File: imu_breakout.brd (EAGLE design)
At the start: 29.5 x 20.7 mm, 11 parts, among them IC1 FT232RL, U1 AHRS8P_CONN, U2 USB-MICROB

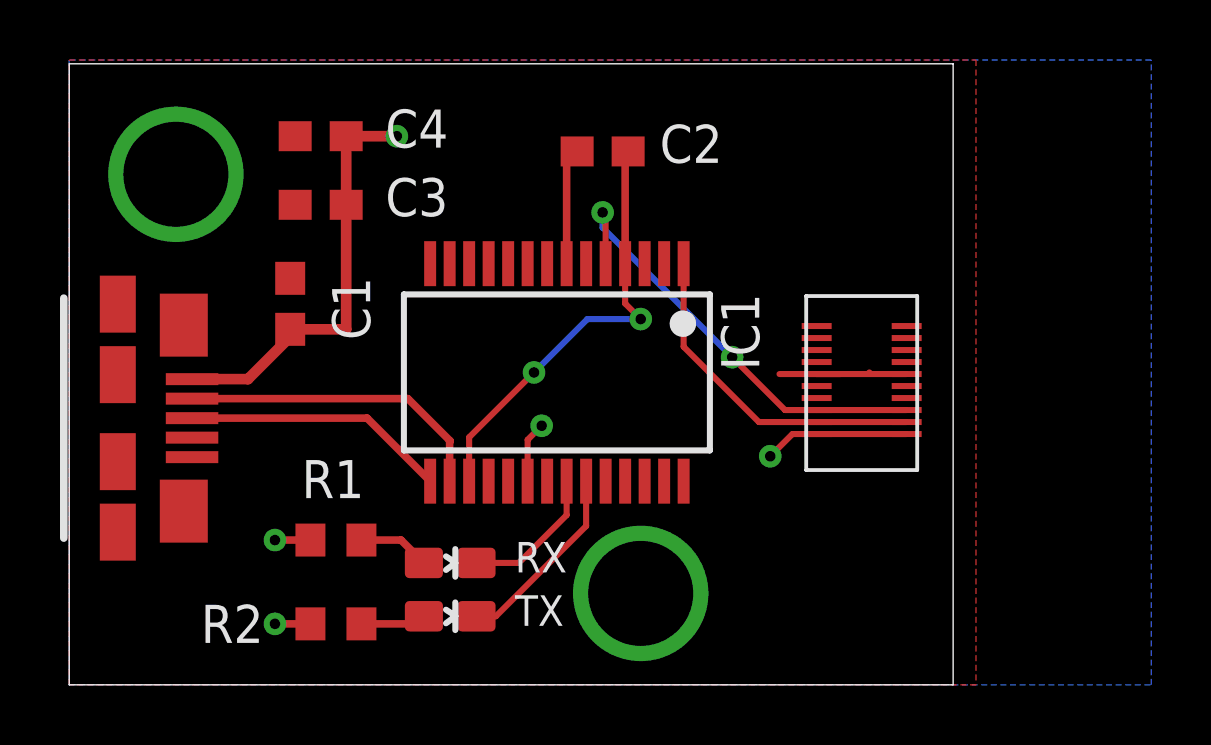
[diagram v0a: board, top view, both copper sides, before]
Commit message: Make pads on ss4 connector longer
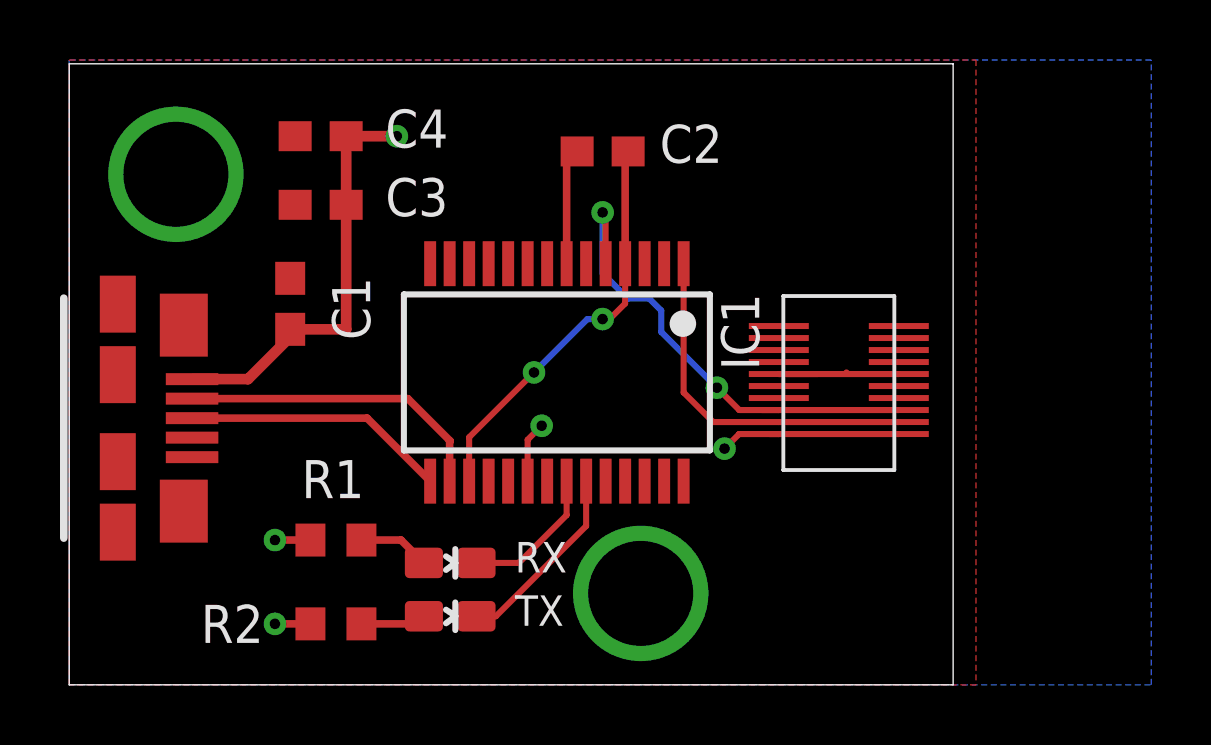
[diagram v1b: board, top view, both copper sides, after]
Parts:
- moved U1 0.76 mm to (25.7, 10.2)
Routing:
- net IMU_TX: track 14.9 -> 16.5 mm
- net 5V: track 23.7 -> 25.2 mm
- net 3V3OUT: track 14.7 -> 13.6 mm
- net IMU_RX: track 11.2 -> 11.9 mm
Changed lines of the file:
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@@
 <?xml version="1.0" encoding="utf-8"?>
 <!DOCTYPE eagle SYSTEM "eagle.dtd">
-<eagle version="8.7.1">
+<eagle version="9.0.1">
 <drawing>
 <settings>
@@
 <attribute name="NAME" x="14.859" y="1.9685" size="1.016" layer="25" font="vector"/>
 </element>
-<element name="U1" library="auv" package="ST4-10-1.00-L-D-P-TR" value="AHRS8P_CONN" x="26.416" y="10.16" rot="R270"/>
+<element name="U1" library="auv" package="ST4-10-1.00-L-D-P-TR" value="AHRS8P_CONN" x="25.654" y="10.16" rot="R270"/>
 <element name="U2" library="auv" package="USB-B-MICRO-SMD" value="USB-MICROB" x="1.27" y="8.89" rot="R270"/>
 </elements>
@@
 <contactref element="U1" pad="3"/>
 <contactref element="U1" pad="4"/>
-<wire x1="24.916" y1="8.76" x2="27.916" y2="8.76" width="0.2032" layer="1"/>
-<wire x1="24.916" y1="8.76" x2="22.99" y2="8.76" width="0.2032" layer="1"/>
-<wire x1="20.481" y1="11.269" x2="20.481" y2="14.039" width="0.2032" layer="1"/>
-<wire x1="22.99" y1="8.76" x2="20.481" y2="11.269" width="0.2032" layer="1"/>
+<wire x1="23.654" y1="8.76" x2="27.654" y2="8.76" width="0.2032" layer="1"/>
+<wire x1="23.654" y1="8.76" x2="21.466" y2="8.76" width="0.2032" layer="1"/>
+<wire x1="21.466" y1="8.76" x2="20.481" y2="9.745" width="0.2032" layer="1"/>
+<wire x1="20.481" y1="9.745" x2="20.481" y2="14.039" width="0.2032" layer="1"/>
 </signal>
 <signal name="IMU_TX">
@@
 <contactref element="U1" pad="5"/>
 <contactref element="U1" pad="6"/>
-<wire x1="24.916" y1="9.16" x2="27.916" y2="9.16" width="0.2032" layer="1"/>
-<wire x1="24.916" y1="9.16" x2="23.86" y2="9.16" width="0.2032" layer="1"/>
-<wire x1="23.86" y1="9.16" x2="22.098" y2="10.922" width="0.2032" layer="1"/>
-<via x="22.098" y="10.922" extent="1-16" drill="0.35"/>
-<wire x1="22.098" y1="10.922" x2="17.78" y2="15.24" width="0.2032" layer="16"/>
-<wire x1="17.78" y1="15.24" x2="17.78" y2="15.748" width="0.2032" layer="16"/>
+<wire x1="23.654" y1="9.16" x2="27.654" y2="9.16" width="0.2032" layer="1"/>
+<wire x1="23.654" y1="9.16" x2="23.098" y2="9.16" width="0.2032" layer="1"/>
 <via x="17.78" y="15.748" extent="1-16" drill="0.35"/>
 <wire x1="17.78" y1="15.748" x2="17.881" y2="15.647" width="0.2032" layer="1"/>
 <wire x1="17.881" y1="15.647" x2="17.881" y2="14.039" width="0.2032" layer="1"/>
+<wire x1="23.654" y1="9.16" x2="22.336" y2="9.16" width="0.2032" layer="1"/>
+<wire x1="22.336" y1="9.16" x2="21.59" y2="9.906" width="0.2032" layer="1"/>
+<via x="21.59" y="9.906" extent="1-16" drill="0.35"/>
+<wire x1="19.7348" y1="12.47565625" x2="19.33365625" y2="12.8768" width="0.2032" layer="16"/>
+<wire x1="21.59" y1="9.906" x2="19.7348" y2="11.7612" width="0.2032" layer="16"/>
+<wire x1="18.6192" y1="12.8768" x2="17.78" y2="13.716" width="0.2032" layer="16"/>
+<wire x1="19.7348" y1="11.7612" x2="19.7348" y2="12.47565625" width="0.2032" layer="16"/>
+<wire x1="19.33365625" y1="12.8768" x2="18.6192" y2="12.8768" width="0.2032" layer="16"/>
+<wire x1="17.78" y1="13.716" x2="17.78" y2="15.748" width="0.2032" layer="16"/>
 </signal>
 <signal name="GND">
@@
 <vertex x="0" y="0"/>
 </polygon>
-<wire x1="24.916" y1="10.36" x2="25.708" y2="10.36" width="0.2032" layer="1"/>
-<wire x1="26.724" y1="10.36" x2="26.67" y2="10.414" width="0.2032" layer="1"/>
-<wire x1="24.916" y1="10.36" x2="23.676" y2="10.36" width="0.2032" layer="1"/>
-<wire x1="24.916" y1="10.36" x2="27.916" y2="10.36" width="0.2032" layer="1"/>
+<wire x1="23.654" y1="10.36" x2="24.946" y2="10.36" width="0.2032" layer="1"/>
+<wire x1="25.962" y1="10.36" x2="25.908" y2="10.414" width="0.2032" layer="1"/>
+<wire x1="23.654" y1="10.36" x2="27.654" y2="10.36" width="0.2032" layer="1"/>
 </signal>
 <signal name="USBDP">
@@
 <via x="15.494" y="10.414" extent="1-16" drill="0.35"/>
 <wire x1="15.494" y1="10.414" x2="17.272" y2="12.192" width="0.2032" layer="16"/>
-<wire x1="17.272" y1="12.192" x2="19.05" y2="12.192" width="0.2032" layer="16"/>
-<via x="19.05" y="12.192" extent="1-16" drill="0.35"/>
-<wire x1="19.05" y1="12.192" x2="18.531" y2="12.711" width="0.2032" layer="1"/>
 <wire x1="18.531" y1="12.711" x2="18.531" y2="14.039" width="0.2032" layer="1"/>
+<wire x1="17.272" y1="12.192" x2="17.78" y2="12.192" width="0.2032" layer="16"/>
+<via x="17.78" y="12.192" extent="1-16" drill="0.35"/>
+<wire x1="17.78" y1="12.192" x2="18.012" y2="12.192" width="0.2032" layer="1"/>
+<wire x1="18.012" y1="12.192" x2="18.531" y2="12.711" width="0.2032" layer="1"/>
 </signal>
 <signal name="5V">
@@
 </polygon>
 <wire x1="7.366" y1="11.85" x2="7.62" y2="11.85" width="0.3556" layer="1"/>
-<wire x1="24.916" y1="8.36" x2="27.916" y2="8.36" width="0.2032" layer="1"/>
+<wire x1="23.654" y1="8.36" x2="27.654" y2="8.36" width="0.2032" layer="1"/>
 <wire x1="15.281" y1="6.789" x2="15.281" y2="8.169" width="0.2032" layer="1"/>
 <wire x1="15.281" y1="8.169" x2="15.748" y2="8.636" width="0.2032" layer="1"/>
@@
 <wire x1="4.095" y1="10.19" x2="5.96" y2="10.19" width="0.3556" layer="1"/>
 <wire x1="5.96" y1="10.19" x2="7.62" y2="11.85" width="0.3556" layer="1"/>
-<wire x1="24.916" y1="8.36" x2="24.108" y2="8.36" width="0.2032" layer="1"/>
-<wire x1="24.108" y1="8.36" x2="23.368" y2="7.62" width="0.2032" layer="1"/>
-<via x="23.368" y="7.62" extent="1-16" drill="0.35"/>
+<wire x1="23.654" y1="8.36" x2="23.346" y2="8.36" width="0.2032" layer="1"/>
 <wire x1="9.232" y1="16.002" x2="9.232" y2="18.288" width="0.3556" layer="1"/>
 <wire x1="7.366" y1="11.85" x2="9.232" y2="11.85" width="0.3556" layer="1"/>
@@
 <wire x1="9.232" y1="18.288" x2="10.922" y2="18.288" width="0.3556" layer="1"/>
 <via x="10.922" y="18.288" extent="1-16" drill="0.35"/>
+<wire x1="23.654" y1="8.36" x2="22.33" y2="8.36" width="0.2032" layer="1"/>
+<wire x1="22.33" y1="8.36" x2="21.844" y2="7.874" width="0.2032" layer="1"/>
+<via x="21.844" y="7.874" extent="1-16" drill="0.35"/>
 </signal>
 <signal name="N$6">

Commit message: Add auv logo
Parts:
- added U$1: (no value), auv:ILLINOISAUV
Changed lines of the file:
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@@
 <element name="U1" library="auv" package="ST4-10-1.00-L-D-P-TR" value="AHRS8P_CONN" x="25.654" y="10.16" rot="R270"/>
 <element name="U2" library="auv" package="USB-B-MICRO-SMD" value="USB-MICROB" x="1.27" y="8.89" rot="R270"/>
+<element name="U$1" library="auv" package="ILLINOISAUV" value="" x="14.224" y="9.144" rot="MR270"/>
 </elements>
 <signals>
